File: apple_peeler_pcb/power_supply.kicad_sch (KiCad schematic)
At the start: 14 parts, among them U4 TPS562242

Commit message: use wleds instead of individual leds
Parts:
- renumbered R40 to R35, R41 to R36, R42 to R37
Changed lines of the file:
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@@
 		(on_board yes)
 		(dnp no)
-		(property "Reference" "R40"
+		(property "Reference" "R35"
 			(at 152.4 85.0899 0)
 			(effects
@@
 			(project "apple_peeler_pcb"
 				(path "/d5946b96-44a8-4a28-8641-19803e1510af/ad50c616-8b19-49c2-9202-d566f63fdad1"
-					(reference "R40")
+					(reference "R35")
 					(unit 1)
 				)
@@
 		(dnp no)
 		(fields_autoplaced yes)
-		(property "Reference" "#PWR066"
+		(property "Reference" "#PWR061"
 			(at 175.26 97.79 0)
 			(effects
@@
 			(project "apple_peeler_pcb"
 				(path "/d5946b96-44a8-4a28-8641-19803e1510af/ad50c616-8b19-49c2-9202-d566f63fdad1"
-					(reference "#PWR066")
+					(reference "#PWR061")
 					(unit 1)
 				)
@@
 		(on_board yes)
 		(dnp no)
-		(property "Reference" "R41"
+		(property "Reference" "R36"
 			(at 152.4 93.9799 0)
 			(effects
@@
 			(project "apple_peeler_pcb"
 				(path "/d5946b96-44a8-4a28-8641-19803e1510af/ad50c616-8b19-49c2-9202-d566f63fdad1"
-					(reference "R41")
+					(reference "R36")
 					(unit 1)
 				)
@@
 		(dnp no)
 		(fields_autoplaced yes)
-		(property "Reference" "#PWR061"
+		(property "Reference" "#PWR056"
 			(at 88.9 97.79 0)
 			(effects
@@
 			(project "apple_peeler_pcb"
 				(path "/d5946b96-44a8-4a28-8641-19803e1510af/ad50c616-8b19-49c2-9202-d566f63fdad1"
-					(reference "#PWR061")
+					(reference "#PWR056")
 					(unit 1)
 				)
@@
 		(dnp no)
 		(fields_autoplaced yes)
-		(property "Reference" "#PWR067"
+		(property "Reference" "#PWR062"
 			(at 185.42 97.79 0)
 			(effects
@@
 			(project "apple_peeler_pcb"
 				(path "/d5946b96-44a8-4a28-8641-19803e1510af/ad50c616-8b19-49c2-9202-d566f63fdad1"
-					(reference "#PWR067")
+					(reference "#PWR062")
 					(unit 1)
 				)
@@
 		(dnp no)
 		(fields_autoplaced yes)
-		(property "Reference" "#PWR062"
+		(property "Reference" "#PWR057"
 			(at 99.06 97.79 0)
 			(effects
@@
 			(project "apple_peeler_pcb"
 				(path "/d5946b96-44a8-4a28-8641-19803e1510af/ad50c616-8b19-49c2-9202-d566f63fdad1"
-					(reference "#PWR062")
+					(reference "#PWR057")
 					(unit 1)
 				)
@@
 		(dnp no)
 		(fields_autoplaced yes)
-		(property "Reference" "#PWR065"
+		(property "Reference" "#PWR060"
 			(at 165.1 97.79 0)
 			(effects
@@
 			(project "apple_peeler_pcb"
 				(path "/d5946b96-44a8-4a28-8641-19803e1510af/ad50c616-8b19-49c2-9202-d566f63fdad1"
-					(reference "#PWR065")
+					(reference "#PWR060")
 					(unit 1)
 				)
@@
 		(dnp no)
 		(fields_autoplaced yes)
-		(property "Reference" "#PWR063"
+		(property "Reference" "#PWR058"
 			(at 121.92 97.79 0)
 			(effects
@@
 			(project "apple_peeler_pcb"
 				(path "/d5946b96-44a8-4a28-8641-19803e1510af/ad50c616-8b19-49c2-9202-d566f63fdad1"
-					(reference "#PWR063")
+					(reference "#PWR058")
 					(unit 1)
 				)
@@
 		(on_board yes)
 		(dnp no)
-		(property "Reference" "R42"
+		(property "Reference" "R37"
 			(at 152.4 104.1399 0)
 			(effects
@@
 			(project "apple_peeler_pcb"
 				(path "/d5946b96-44a8-4a28-8641-19803e1510af/ad50c616-8b19-49c2-9202-d566f63fdad1"
-					(reference "R42")
+					(reference "R37")
 					(unit 1)
 				)
@@
 		(dnp no)
 		(fields_autoplaced yes)
-		(property "Reference" "#PWR064"
+		(property "Reference" "#PWR059"
 			(at 154.94 116.84 0)
 			(effects
@@
 			(project "apple_peeler_pcb"
 				(path "/d5946b96-44a8-4a28-8641-19803e1510af/ad50c616-8b19-49c2-9202-d566f63fdad1"
-					(reference "#PWR064")
-					(unit 1)
-				)
+					(reference "#PWR059")
+					(unit 1)
+				)

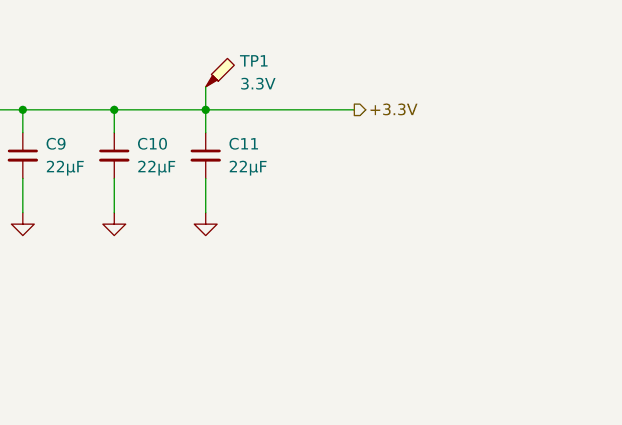
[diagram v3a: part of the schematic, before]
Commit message: fix connector labels and misc silkscreen
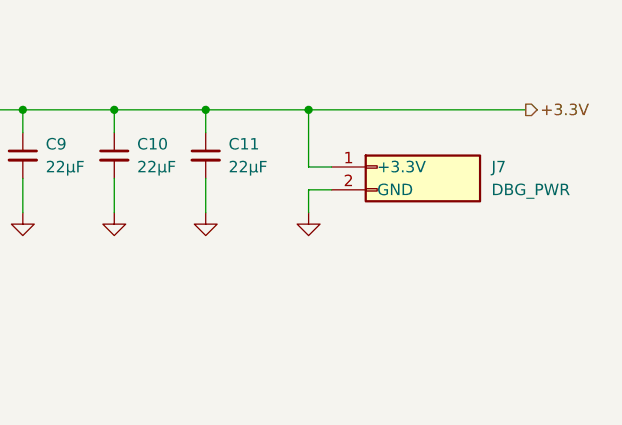
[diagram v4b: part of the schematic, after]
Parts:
- removed TP1: 3.3V, TestPoint:TestPoint_THTPad_2.0x2.0mm_Drill1.0mm, symbol Connector:TestPoint_Probe
- added J7: Header_01x02, conn:PinHeader_1x02_P2.54mm_Vertical, symbol conn:Conn_01x02
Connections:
- net +3.3V: now also J7.1 (Pin_1)
- net GND: now also J7.2 (Pin_2)
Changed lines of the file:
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@@
+	)
+	(junction
+		(at 196.85 80.01)
+		(diameter 0)
+		(color 0 0 0 0)
 	)
 	(junction
@@
 	(wire
 		(pts
-			(xy 185.42 77.47) (xy 185.42 80.01)
-		)
-		(stroke
-			(width 0)
-			(type default)
-		)
-	)
-	(wire
-		(pts
 			(xy 165.1 80.01) (xy 175.26 80.01)
 		)
@@
 	(wire
 		(pts
+			(xy 196.85 88.9) (xy 199.39 88.9)
+		)
+		(stroke
+			(width 0)
+			(type default)
+		)
+	)
+	(wire
+		(pts
 			(xy 154.94 110.49) (xy 154.94 109.22)
 		)
@@
 	(wire
 		(pts
+			(xy 196.85 91.44) (xy 196.85 88.9)
+		)
+		(stroke
+			(width 0)
+			(type default)
+		)
+	)
+	(wire
+		(pts
 			(xy 88.9 71.12) (xy 88.9 80.01)
 		)
@@
 	(wire
 		(pts
-			(xy 185.42 80.01) (xy 201.93 80.01)
+			(xy 185.42 80.01) (xy 196.85 80.01)
 		)
 		(stroke
@@
 	(wire
 		(pts
+			(xy 196.85 80.01) (xy 220.98 80.01)
+		)
+		(stroke
+			(width 0)
+			(type default)
+		)
+	)
+	(wire
+		(pts
 			(xy 72.39 90.17) (xy 78.74 90.17)
 		)
@@
 	(wire
 		(pts
+			(xy 196.85 86.36) (xy 196.85 80.01)
+		)
+		(stroke
+			(width 0)
+			(type default)
+		)
+	)
+	(wire
+		(pts
 			(xy 165.1 87.63) (xy 165.1 91.44)
+		)
+		(stroke
+			(width 0)
+			(type default)
+		)
+	)
+	(wire
+		(pts
+			(xy 199.39 86.36) (xy 196.85 86.36)
 		)
 		(stroke
@@
 	(hierarchical_label "+3.3V"
 		(shape output)
-		(at 201.93 80.01 0)
+		(at 220.98 80.01 0)
 		(effects
 			(font
@@
 	)
 	(symbol
+		(lib_id "conn:Conn_01x02")
+		(at 204.47 88.9 0)
+		(unit 1)
+		(exclude_from_sim no)
+		(in_bom yes)
+		(on_board yes)
+		(dnp no)
+		(fields_autoplaced yes)
+		(property "Reference" "J7"
+			(at 217.17 86.3599 0)
+			(effects
+				(font
+					(size 1.27 1.27)
+				)
+				(justify left)
+			)
+		)
+		(property "Value" "Header_01x02"
+			(at 209.042 91.44 0)
+			(effects
+				(font
+					(size 1.27 1.27)
+				)
+				(hide yes)
+			)
+		)
+		(property "Footprint" "conn:PinHeader_1x02_P2.54mm_Vertical"
+			(at 204.47 88.9 0)
+			(effects
+				(font
+					(size 1.27 1.27)
+				)
+				(hide yes)
+			)
+		)
+		(property "Datasheet" "~"
+			(at 204.47 88.9 0)
+			(effects
+				(font
+					(size 1.27 1.27)
+				)
+				(hide yes)
+			)
+		)
+		(property "Description" "Generic connector, single row, 01x06, script generated (kicad-library-utils/schlib/autogen/connector/)"
+			(at 204.47 88.9 0)
+			(effects
+				(font
+					(size 1.27 1.27)
+				)
+				(hide yes)
+			)
+		)
+		(property "Purpose Pin1" "+3.3V"
+			(at 204.47 86.36 0)
+			(do_not_autoplace yes)
+			(effects
+				(font
+					(size 1.27 1.27)
+				)
+				(justify left)
+			)
+		)
+		(property "Purpose Pin2" "GND"
+			(at 204.47 88.9 0)
+			(do_not_autoplace yes)
+			(effects
+				(font
+					(size 1.27 1.27)
+				)
+				(justify left)
+			)
+		)
+		(property "Purpose" "DBG_PWR"
+			(at 217.17 88.8999 0)
+			(effects
+				(font
+					(size 1.27 1.27)
+				)
+				(justify left)
+			)
+		)
+		(pin "1"
+		)
+		(pin "2"
+		)
+		(instances
+			(project ""
+				(path "/d5946b96-44a8-4a28-8641-19803e1510af/ad50c616-8b19-49c2-9202-d566f63fdad1"
+					(reference "J7")
+					(unit 1)
+				)
+			)
+		)
+	)
+	(symbol
 		(lib_id "Device:R")
 		(at 154.94 95.25 0)
@@
 	)
 	(symbol
+		(lib_id "power:GND")
+		(at 196.85 91.44 0)
+		(unit 1)
+		(exclude_from_sim no)
+		(in_bom yes)
+		(on_board yes)
+		(dnp no)
+		(fields_autoplaced yes)
+		(property "Reference" "#PWR066"
+			(at 196.85 97.79 0)
+			(effects
+				(font
+					(size 1.27 1.27)
+				)
+				(hide yes)
+			)
+		)
+		(property "Value" "GND"
+			(at 196.85 96.52 0)
+			(effects
+				(font
+					(size 1.27 1.27)
+				)
+				(hide yes)
+			)
+		)
+		(property "Footprint" ""
+			(at 196.85 91.44 0)
+			(effects
+				(font
+					(size 1.27 1.27)
+				)
+				(hide yes)
+			)
+		)
+		(property "Datasheet" ""
+			(at 196.85 91.44 0)
+			(effects
+				(font
+					(size 1.27 1.27)
+				)
+				(hide yes)
+			)
+		)
+		(property "Description" "Power symbol creates a global label with name \"GND\" , ground"
+			(at 196.85 91.44 0)
+			(effects
+				(font
+					(size 1.27 1.27)
+				)
+				(hide yes)
+			)
+		)
+		(pin "1"
+		)
+		(instances
+			(project "apple_peeler_pcb"
+				(path "/d5946b96-44a8-4a28-8641-19803e1510af/ad50c616-8b19-49c2-9202-d566f63fdad1"
+					(reference "#PWR066")
+					(unit 1)
+				)
+			)
+		)
+	)
+	(symbol
 		(lib_id "power:PWR_FLAG")
 		(at 154.94 78.74 0)
@@
 					(unit 1)
 				)
-			)
-		)
-	)
-	(symbol
-		(lib_id "Connector:TestPoint_Probe")
-		(at 185.42 77.47 0)
-		(unit 1)
-		(exclude_from_sim no)
-		(in_bom no)
-		(on_board yes)
-		(dnp no)
-		(fields_autoplaced yes)
-		(property "Reference" "TP1"
-			(at 189.23 74.6124 0)
-			(effects
-				(font
-					(size 1.27 1.27)
-				)
-				(justify left)
-			)
-		)
-		(property "Value" "3.3V"
-			(at 189.23 77.1524 0)
-			(effects
-				(font
-					(size 1.27 1.27)
-				)
-				(justify left)
-			)
-		)
-		(property "Footprint" "TestPoint:TestPoint_THTPad_2.0x2.0mm_Drill1.0mm"
-			(at 190.5 77.47 0)
-			(effects
-				(font
-					(size 1.27 1.27)
-				)
-				(hide yes)
-			)
-		)
-		(property "Datasheet" "~"
-			(at 190.5 77.47 0)
-			(effects
-				(font
-					(size 1.27 1.27)
-				)
-				(hide yes)
-			)
-		)
-		(property "Description" "test point (alternative probe-style design)"
-			(at 185.42 77.47 0)
-			(effects
-				(font
-					(size 1.27 1.27)
-				)
-				(hide yes)
-			)
-		)
-		(pin "1"
-		)
-		(instances
-			(project "apple_peeler_pcb"
-				(path "/d5946b96-44a8-4a28-8641-19803e1510af/ad50c616-8b19-49c2-9202-d566f63fdad1"
-					(reference "TP1")
-					(unit 1)
-				)

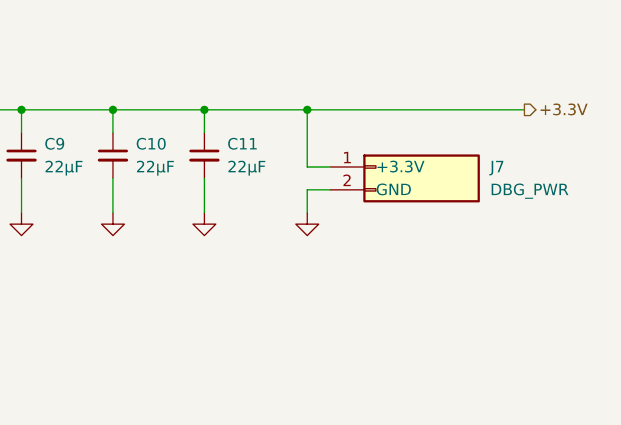
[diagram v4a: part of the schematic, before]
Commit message: change HDMI connector to one that's in stock
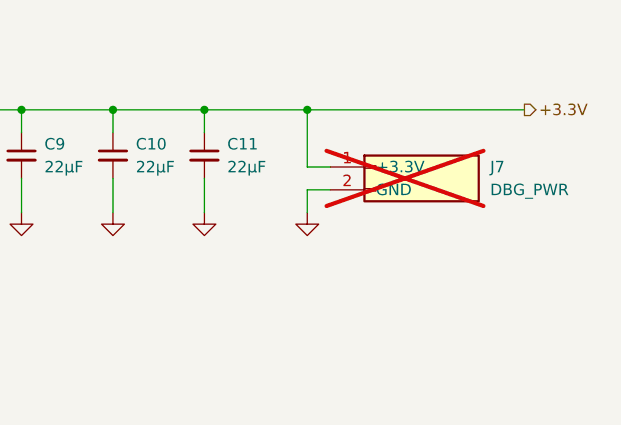
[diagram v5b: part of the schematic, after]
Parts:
- J7: now not fitted
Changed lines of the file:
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@@
 		(in_bom yes)
 		(on_board yes)
-		(dnp no)
+		(dnp yes)
 		(fields_autoplaced yes)
 		(property "Reference" "J7"

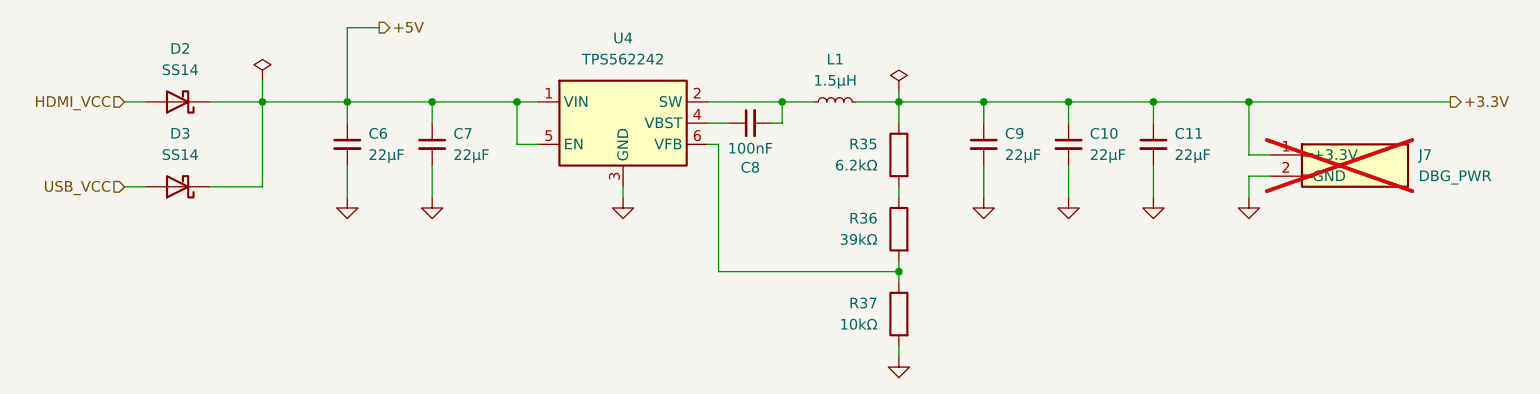
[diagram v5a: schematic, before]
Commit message: update SMPS inductor and divider
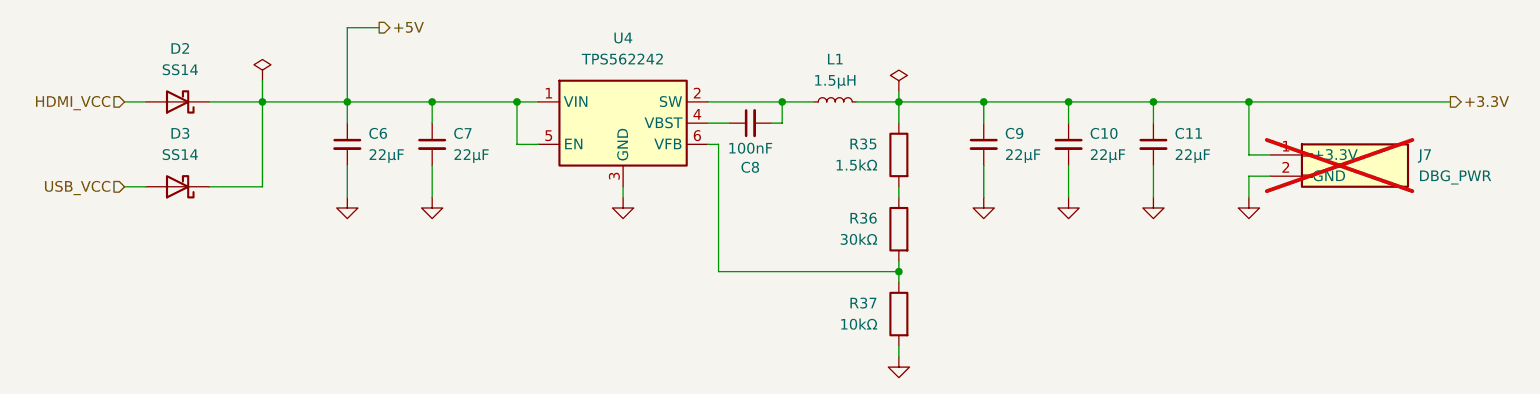
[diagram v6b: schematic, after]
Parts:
- L1: footprint Inductor_SMD:L_Taiyo-Yuden_MD-5050 -> Inductor_SMD:L_Sunlord_SWPA5020S; LCSC C702825 -> C56803; MPN BWVF005050201R5T00 -> SWPA5020S1R5MT
- R35: value 6.2kΩ -> 1.5kΩ; LCSC C17767 -> C4310; MPN R 6.2kΩ 125mW 0805 -> R 1.5kΩ 125mW 0805
- R36: value 39kΩ -> 30kΩ; LCSC C25826 -> C17621; MPN R 39kΩ 125mW 0805 -> R 30kΩ 125mW 0805
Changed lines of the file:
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@@
 			)
 		)
-		(property "Value" "6.2kΩ"
+		(property "Value" "1.5kΩ"
 			(at 152.4 87.6299 0)
 			(effects
@@
 			)
 		)
-		(property "LCSC" "C17767"
+		(property "LCSC" "C4310"
 			(at 154.94 86.36 0)
 			(effects
@@
 			)
 		)
-		(property "MPN" "R 6.2kΩ 125mW 0805"
+		(property "MPN" "R 1.5kΩ 125mW 0805"
 			(at 154.94 86.36 0)
 			(effects
@@
 			)
 		)
-		(property "Value" "39kΩ"
+		(property "Value" "30kΩ"
 			(at 152.4 96.5199 0)
 			(effects
@@
 			)
 		)
-		(property "LCSC" "C25826"
+		(property "LCSC" "C17621"
 			(at 154.94 95.25 0)
 			(effects
@@
 			)
 		)
-		(property "MPN" "R 39kΩ 125mW 0805"
+		(property "MPN" "R 30kΩ 125mW 0805"
 			(at 154.94 95.25 0)
 			(effects
@@
 			)
 		)
-		(property "Footprint" "Inductor_SMD:L_Taiyo-Yuden_MD-5050"
+		(property "Footprint" "Inductor_SMD:L_Sunlord_SWPA5020S"
 			(at 147.32 80.01 0)
 			(effects
@@
 			)
 		)
-		(property "LCSC" "C702825"
+		(property "LCSC" "C56803"
 			(at 147.32 80.01 90)
 			(effects
@@
 			)
 		)
-		(property "MPN" "BWVF005050201R5T00"
+		(property "MPN" "SWPA5020S1R5MT"
 			(at 147.32 80.01 90)
 			(effects

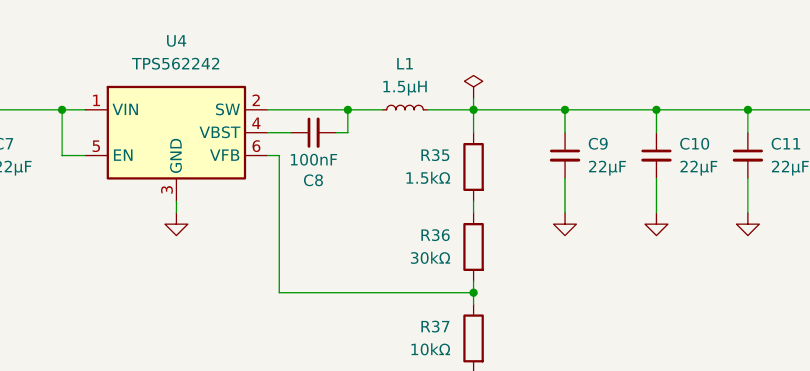
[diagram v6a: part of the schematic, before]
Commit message: correct inductor for smps
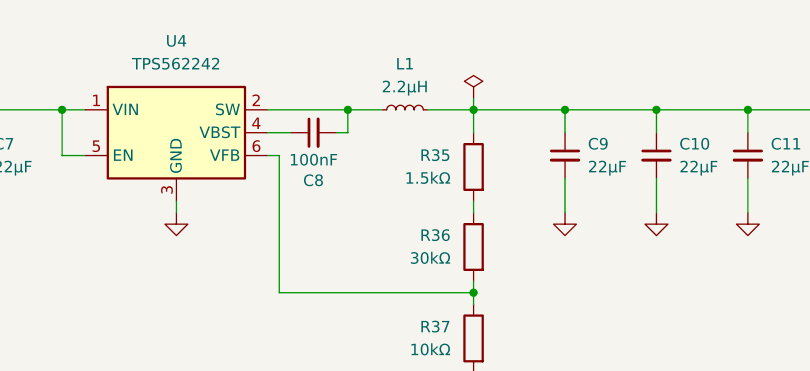
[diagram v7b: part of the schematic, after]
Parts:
- L1: value 1.5μH -> 2.2μH; LCSC C56803 -> C279946; MPN SWPA5020S1R5MT -> SWPA5020S2R2MT
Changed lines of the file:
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@@
 			)
 		)
-		(property "Value" "1.5μH"
+		(property "Value" "2.2μH"
 			(at 147.32 77.47 90)
 			(effects
@@
 			)
 		)
-		(property "LCSC" "C56803"
+		(property "LCSC" "C279946"
 			(at 147.32 80.01 90)
 			(effects
@@
 			)
 		)
-		(property "MPN" "SWPA5020S1R5MT"
+		(property "MPN" "SWPA5020S2R2MT"
 			(at 147.32 80.01 90)
 			(effects

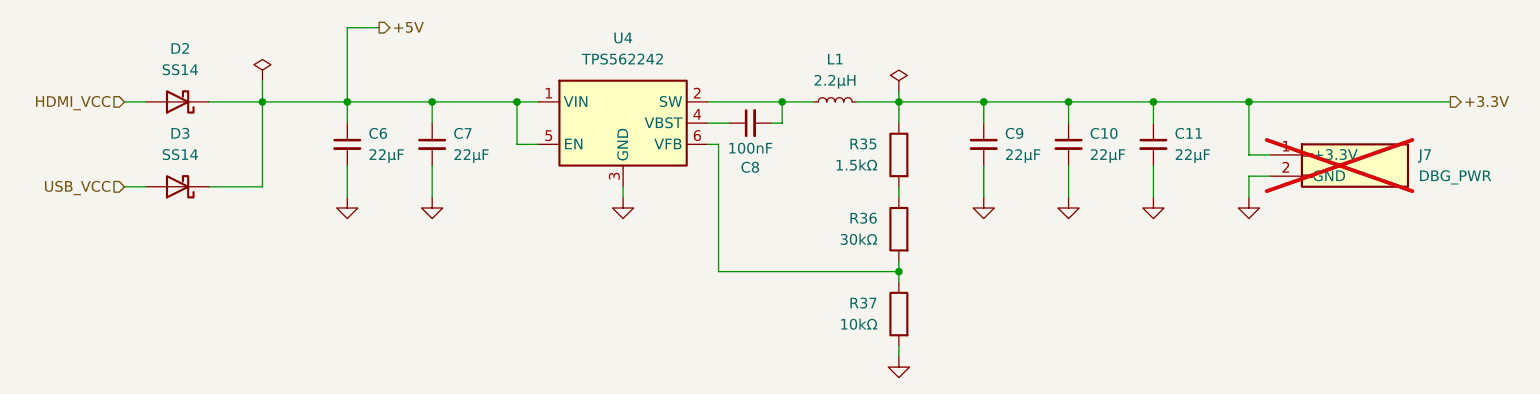
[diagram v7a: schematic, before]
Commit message: replace fancy debug connectors by pin header to save $8
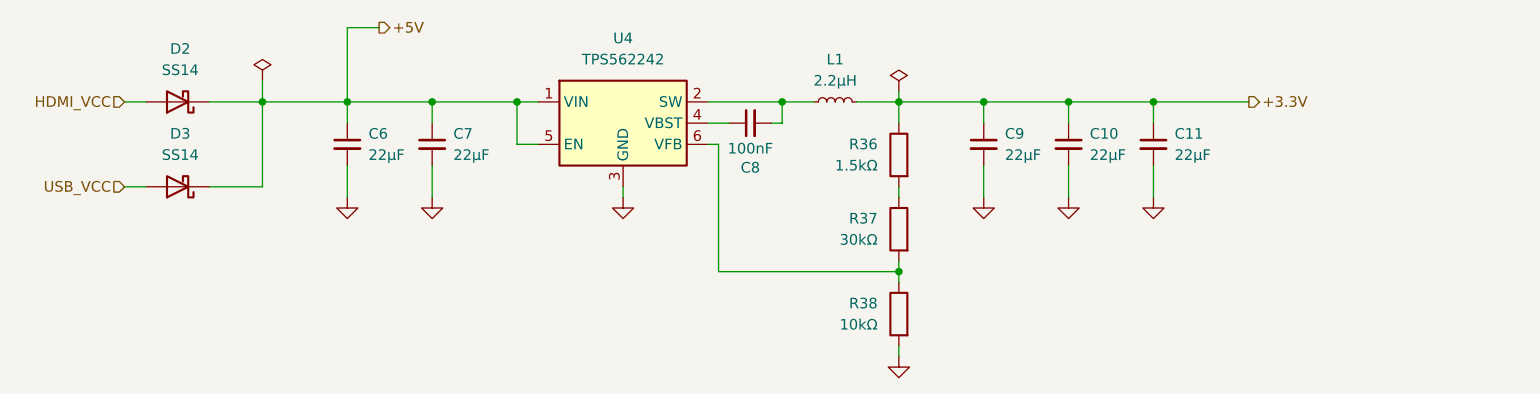
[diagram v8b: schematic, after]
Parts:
- removed J7: Header_01x02, conn:PinHeader_1x02_P2.54mm_Vertical, symbol conn:Conn_01x02
- renumbered R35 to R36, R36 to R37, R37 to R38
